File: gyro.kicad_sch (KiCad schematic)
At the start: 0 parts

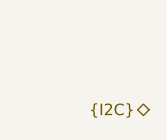
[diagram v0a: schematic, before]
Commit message: Fixed bus names
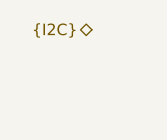
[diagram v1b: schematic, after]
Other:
- title: Pheonix ADXL -> Phoenix Gyro
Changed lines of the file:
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@@
   (paper "A5")
   (title_block
-    (title "Pheonix ADXL")
+    (title "Phoenix Gyro")
   )
-  (hierarchical_label "{I2C}" (shape bidirectional) (at 27.94 29.21 180)
+  (hierarchical_label "{I2C}" (shape bidirectional) (at 21.59 20.32 180)
     (effects (font (size 1.27 1.27)) (justify right))
   )

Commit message: Various updates because I forgot to commit for a while
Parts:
- added C14: 10uF, symbol Device:C
- added C15: 100nF, symbol Device:C
- added U4: I3G4250D, symbol Sensor:I3G4250D
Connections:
- new net +3.3V: C14.1, C15.1, U4.1 (Vdd_IO), U4.15 (RESERVED), U4.16 (VDD), U4.5 (CS)
- new net GND: C14.2, C15.2, U4.10 (RES), U4.11 (RES), U4.12 (RES), U4.13 (GND), U4.4 (SDO/SA0), U4.8 (RES), U4.9 (RES)
- new net Gyro1: U4.7 (INT1)
- new net Gyro2: U4.6 (DRDY/INT2)
- new net SCL: U4.2 (SCL/SPC)
- new net SDA: U4.3 (SDA/SDI/SDO)

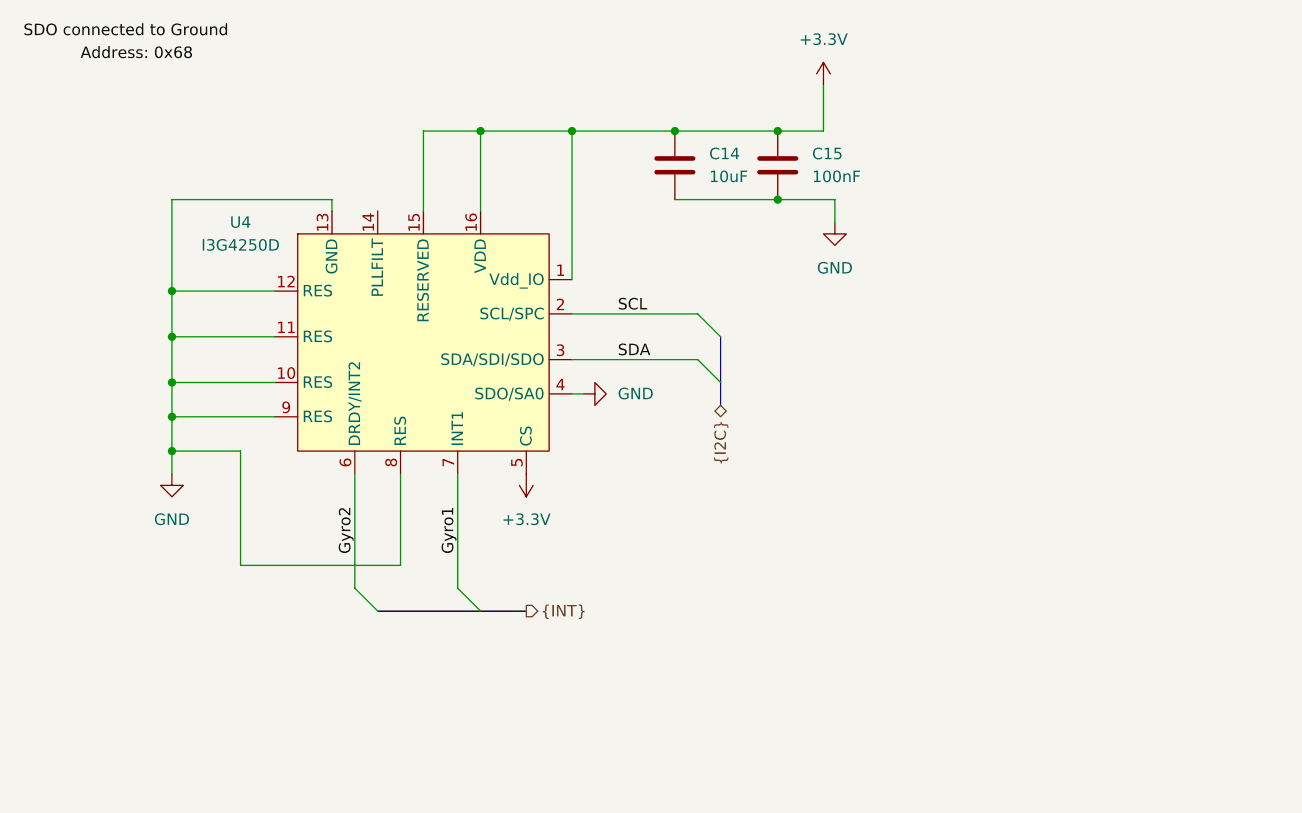
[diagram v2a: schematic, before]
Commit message: Added PLL filter
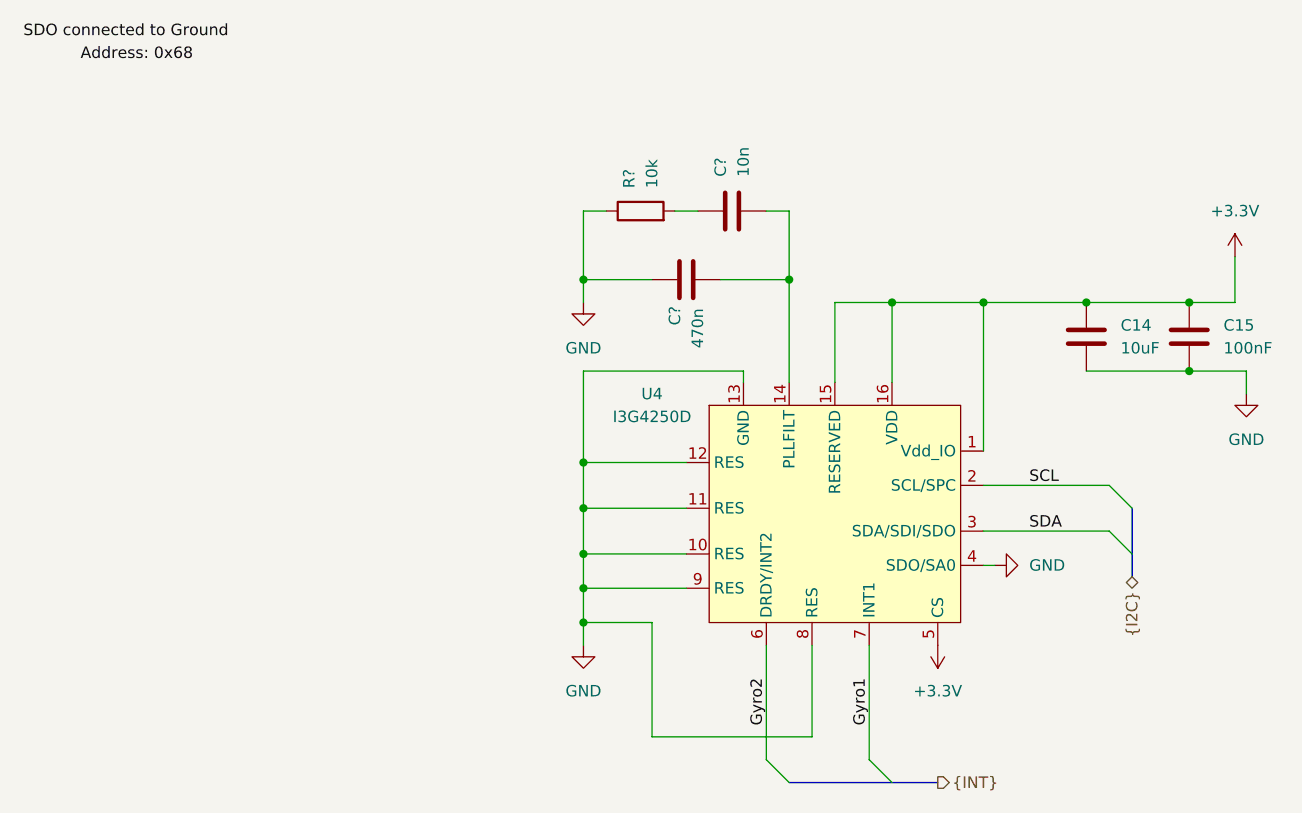
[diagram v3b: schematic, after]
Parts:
- added C?: 470n, Capacitor_SMD:C_0603_1608Metric, symbol Device:C
- added C?: 10n, Capacitor_SMD:C_0603_1608Metric, symbol Device:C
- added R?: 10k, Capacitor_SMD:C_0603_1608Metric, symbol Device:R
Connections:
- net GND: now also C?.1, R?.1
- net at U4.14 (PLLFILT): now also C?.1, C?.2
- new net: C?.2, R?.2
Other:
- moved on the sheet: C14, C15, U4

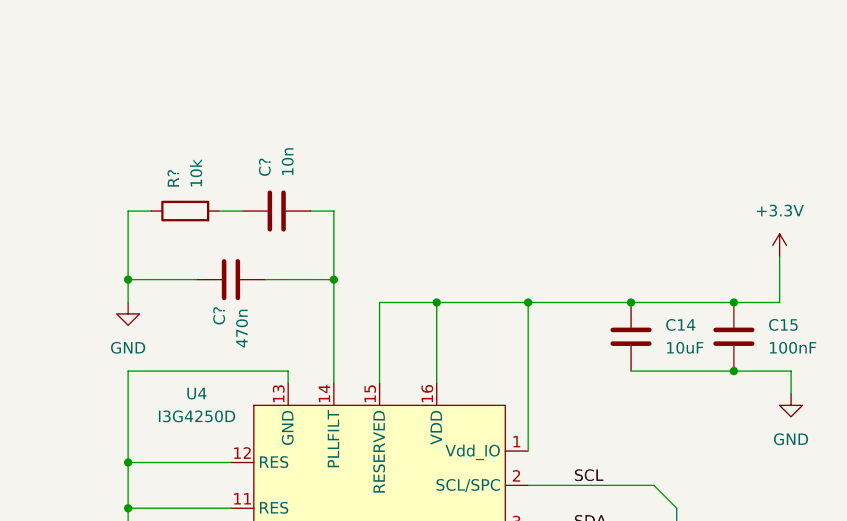
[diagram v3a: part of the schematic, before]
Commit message: Connected the sensors, flash chip, Need to connect the radio and GPS
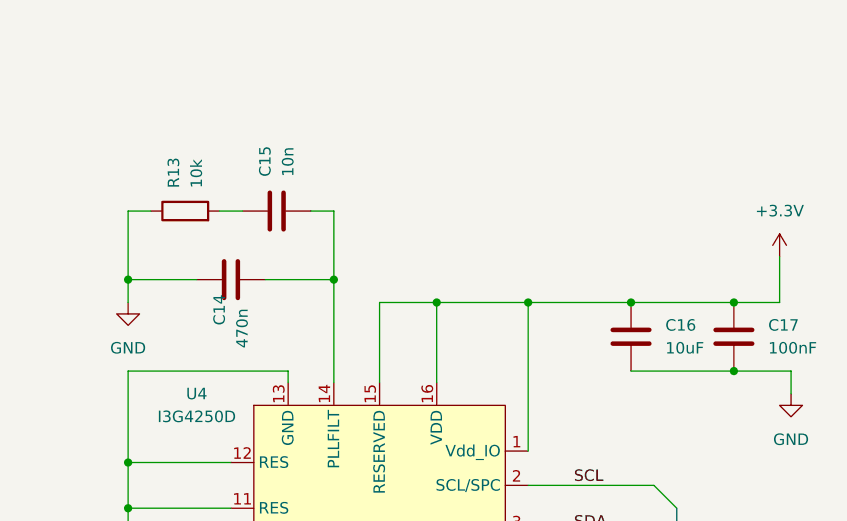
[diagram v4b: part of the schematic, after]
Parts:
- R13: renamed from R?; footprint Capacitor_SMD:C_0603_1608Metric -> Resistor_SMD:R_0603_1608Metric
- U4: footprint (none) -> YAR_Sensors:I3G4250D
- gave numbers to parts that had none: 2
- renumbered C14 to C16, C15 to C17
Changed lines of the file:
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@@
   (symbol (lib_id "power:GND") (at 76.2 83.82 0) (unit 1)
     (in_bom yes) (on_board yes) (fields_autoplaced)
-    (property "Reference" "#PWR027" (id 0) (at 76.2 90.17 0)
+    (property "Reference" "#PWR029" (id 0) (at 76.2 90.17 0)
       (effects (font (size 1.27 1.27)) hide)
     )
@@
   (symbol (lib_id "Device:C") (at 143.51 49.53 0) (unit 1)
     (in_bom yes) (on_board yes)
-    (property "Reference" "C15" (id 0) (at 147.32 48.26 0)
+    (property "Reference" "C17" (id 0) (at 147.32 48.26 0)
       (effects (font (size 1.27 1.27)) (justify left))
     )
@@
   (symbol (lib_id "power:GND") (at 76.2 45.72 0) (unit 1)
     (in_bom yes) (on_board yes) (fields_autoplaced)
-    (property "Reference" "#PWR?" (id 0) (at 76.2 52.07 0)
+    (property "Reference" "#PWR028" (id 0) (at 76.2 52.07 0)
       (effects (font (size 1.27 1.27)) hide)
     )
@@
   (symbol (lib_id "Device:C") (at 132.08 49.53 0) (unit 1)
     (in_bom yes) (on_board yes)
-    (property "Reference" "C14" (id 0) (at 135.89 48.26 0)
+    (property "Reference" "C16" (id 0) (at 135.89 48.26 0)
       (effects (font (size 1.27 1.27)) (justify left))
     )
@@
   (symbol (lib_id "Device:C") (at 87.63 43.18 90) (mirror x) (unit 1)
     (in_bom yes) (on_board yes)
-    (property "Reference" "C?" (id 0) (at 86.36 48.26 0)
+    (property "Reference" "C14" (id 0) (at 86.36 48.26 0)
       (effects (font (size 1.27 1.27)) (justify right))
     )
@@
   (symbol (lib_id "power:GND") (at 149.86 55.88 0) (unit 1)
     (in_bom yes) (on_board yes) (fields_autoplaced)
-    (property "Reference" "#PWR031" (id 0) (at 149.86 62.23 0)
+    (property "Reference" "#PWR033" (id 0) (at 149.86 62.23 0)
       (effects (font (size 1.27 1.27)) hide)
     )
@@
   (symbol (lib_id "Device:C") (at 92.71 35.56 270) (unit 1)
     (in_bom yes) (on_board yes) (fields_autoplaced)
-    (property "Reference" "C?" (id 0) (at 91.4399 31.75 0)
+    (property "Reference" "C15" (id 0) (at 91.4399 31.75 0)
       (effects (font (size 1.27 1.27)) (justify right))
     )
@@
   (symbol (lib_id "Device:R") (at 82.55 35.56 90) (unit 1)
     (in_bom yes) (on_board yes) (fields_autoplaced)
-    (property "Reference" "R?" (id 0) (at 81.2799 33.02 0)
+    (property "Reference" "R13" (id 0) (at 81.2799 33.02 0)
       (effects (font (size 1.27 1.27)) (justify left))
     )
@@
       (effects (font (size 1.27 1.27)) (justify left))
     )
-    (property "Footprint" "Capacitor_SMD:C_0603_1608Metric" (id 2) (at 82.55 37.338 90)
+    (property "Footprint" "Resistor_SMD:R_0603_1608Metric" (id 2) (at 82.55 37.338 90)
       (effects (font (size 1.27 1.27)) hide)
     )
@@
   (symbol (lib_id "power:+3.3V") (at 148.59 40.64 0) (unit 1)
     (in_bom yes) (on_board yes) (fields_autoplaced)
-    (property "Reference" "#PWR030" (id 0) (at 148.59 44.45 0)
+    (property "Reference" "#PWR032" (id 0) (at 148.59 44.45 0)
       (effects (font (size 1.27 1.27)) hide)
     )
@@
   (symbol (lib_id "power:+3.3V") (at 115.57 83.82 180) (unit 1)
     (in_bom yes) (on_board yes) (fields_autoplaced)
-    (property "Reference" "#PWR028" (id 0) (at 115.57 80.01 0)
+    (property "Reference" "#PWR030" (id 0) (at 115.57 80.01 0)
       (effects (font (size 1.27 1.27)) hide)
     )
@@
     (property "Reference" "U4" (id 0) (at 83.82 55.88 0))
     (property "Value" "I3G4250D" (id 1) (at 83.82 58.42 0))
-    (property "Footprint" "" (id 2) (at 97.79 46.99 0)
+    (property "Footprint" "YAR_Sensors:I3G4250D" (id 2) (at 97.79 46.99 0)
       (effects (font (size 1.27 1.27)) hide)
     )
@@
   (symbol (lib_id "power:GND") (at 121.92 74.93 90) (unit 1)
     (in_bom yes) (on_board yes) (fields_autoplaced)
-    (property "Reference" "#PWR029" (id 0) (at 128.27 74.93 0)
+    (property "Reference" "#PWR031" (id 0) (at 128.27 74.93 0)
       (effects (font (size 1.27 1.27)) hide)
     )

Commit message: Rearrange parts of PCB
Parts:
- C16, C17: footprint (none) -> Capacitor_SMD:C_0603_1608Metric
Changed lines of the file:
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@@
       (effects (font (size 1.27 1.27)) (justify left))
     )
-    (property "Footprint" "" (id 2) (at 144.4752 53.34 0)
+    (property "Footprint" "Capacitor_SMD:C_0603_1608Metric" (id 2) (at 144.4752 53.34 0)
       (effects (font (size 1.27 1.27)) hide)
     )
@@
       (effects (font (size 1.27 1.27)) (justify left))
     )
-    (property "Footprint" "" (id 2) (at 133.0452 53.34 0)
+    (property "Footprint" "Capacitor_SMD:C_0603_1608Metric" (id 2) (at 133.0452 53.34 0)
       (effects (font (size 1.27 1.27)) hide)
     )

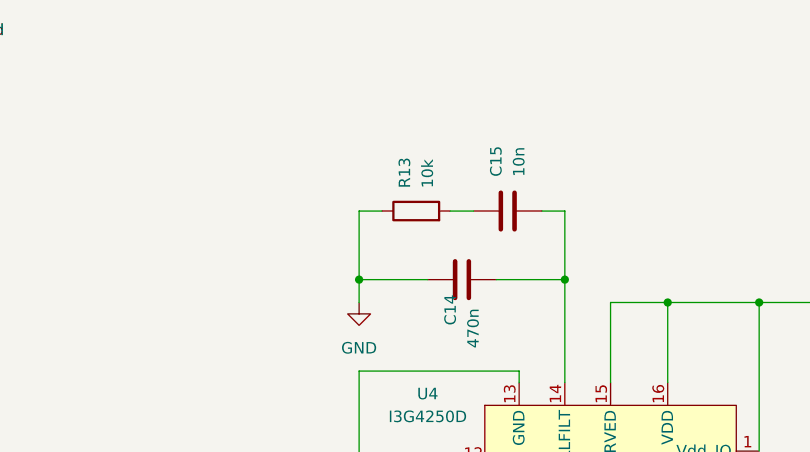
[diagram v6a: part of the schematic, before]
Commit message: Added polyfuse
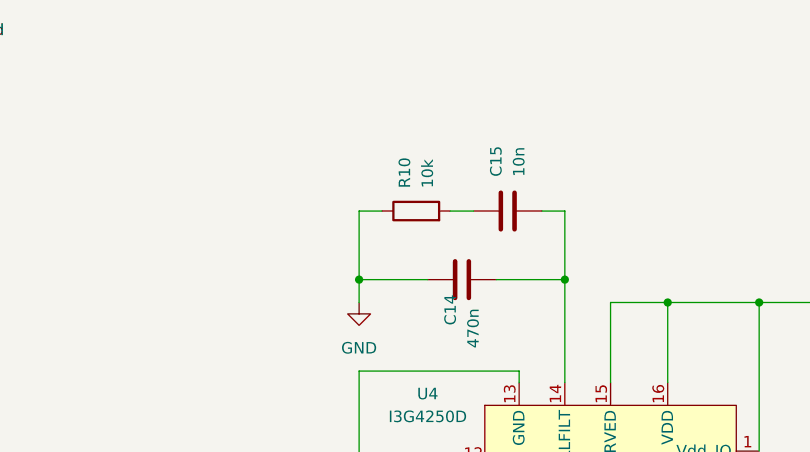
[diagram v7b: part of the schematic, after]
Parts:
- renumbered R13 to R10
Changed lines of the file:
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@@
   (symbol (lib_id "power:GND") (at 76.2 83.82 0) (unit 1)
     (in_bom yes) (on_board yes) (fields_autoplaced)
-    (property "Reference" "#PWR029" (id 0) (at 76.2 90.17 0)
+    (property "Reference" "#PWR027" (id 0) (at 76.2 90.17 0)
       (effects (font (size 1.27 1.27)) hide)
     )
@@
   (symbol (lib_id "power:GND") (at 76.2 45.72 0) (unit 1)
     (in_bom yes) (on_board yes) (fields_autoplaced)
-    (property "Reference" "#PWR028" (id 0) (at 76.2 52.07 0)
+    (property "Reference" "#PWR026" (id 0) (at 76.2 52.07 0)
       (effects (font (size 1.27 1.27)) hide)
     )
@@
   (symbol (lib_id "power:GND") (at 149.86 55.88 0) (unit 1)
     (in_bom yes) (on_board yes) (fields_autoplaced)
-    (property "Reference" "#PWR033" (id 0) (at 149.86 62.23 0)
+    (property "Reference" "#PWR031" (id 0) (at 149.86 62.23 0)
       (effects (font (size 1.27 1.27)) hide)
     )
@@
   (symbol (lib_id "Device:R") (at 82.55 35.56 90) (unit 1)
     (in_bom yes) (on_board yes) (fields_autoplaced)
-    (property "Reference" "R13" (id 0) (at 81.2799 33.02 0)
+    (property "Reference" "R10" (id 0) (at 81.2799 33.02 0)
       (effects (font (size 1.27 1.27)) (justify left))
     )
@@
   (symbol (lib_id "power:+3.3V") (at 148.59 40.64 0) (unit 1)
     (in_bom yes) (on_board yes) (fields_autoplaced)
-    (property "Reference" "#PWR032" (id 0) (at 148.59 44.45 0)
+    (property "Reference" "#PWR030" (id 0) (at 148.59 44.45 0)
       (effects (font (size 1.27 1.27)) hide)
     )
@@
   (symbol (lib_id "power:+3.3V") (at 115.57 83.82 180) (unit 1)
     (in_bom yes) (on_board yes) (fields_autoplaced)
-    (property "Reference" "#PWR030" (id 0) (at 115.57 80.01 0)
+    (property "Reference" "#PWR028" (id 0) (at 115.57 80.01 0)
       (effects (font (size 1.27 1.27)) hide)
     )
@@
   (symbol (lib_id "power:GND") (at 121.92 74.93 90) (unit 1)
     (in_bom yes) (on_board yes) (fields_autoplaced)
-    (property "Reference" "#PWR031" (id 0) (at 128.27 74.93 0)
+    (property "Reference" "#PWR029" (id 0) (at 128.27 74.93 0)
       (effects (font (size 1.27 1.27)) hide)
     )

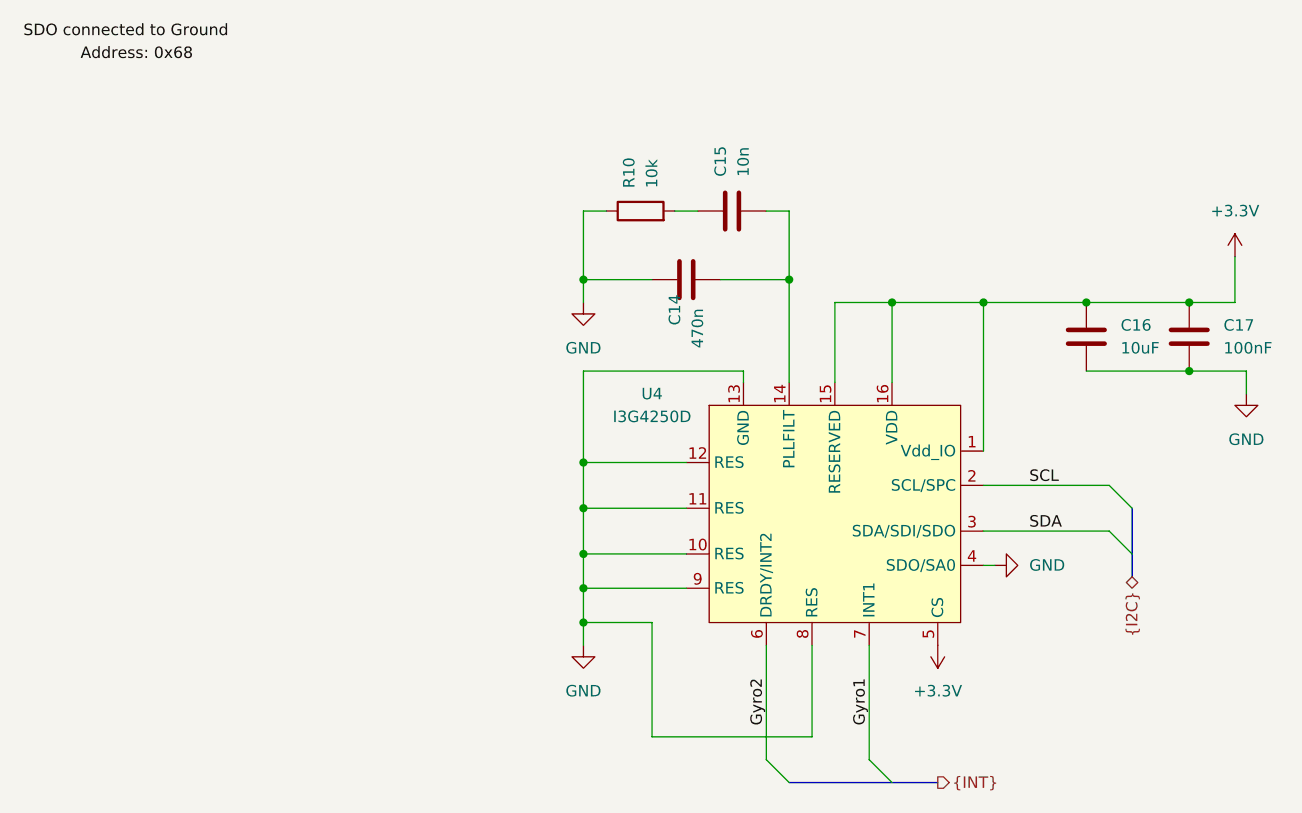
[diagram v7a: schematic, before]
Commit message: Fixed power ports
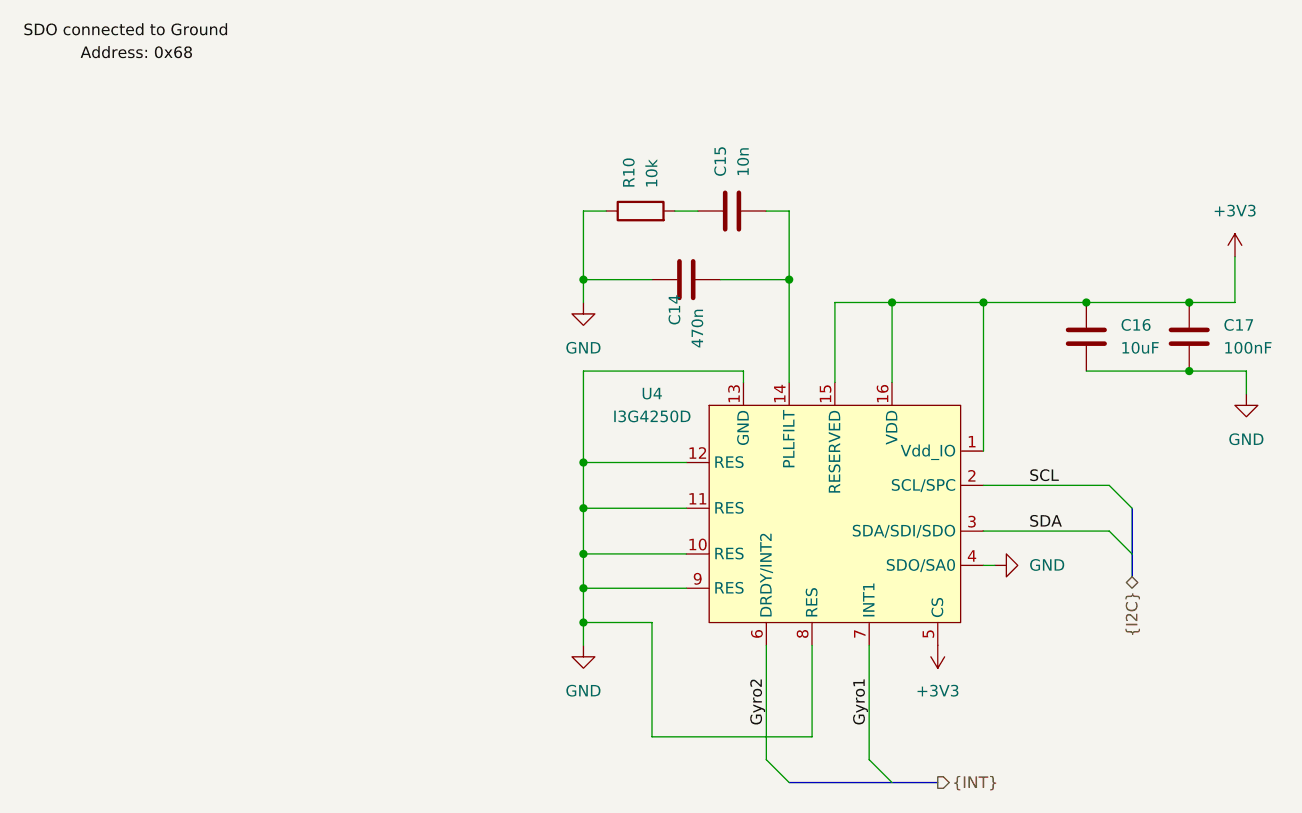
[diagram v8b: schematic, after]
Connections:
- net +3.3V renamed +3V3
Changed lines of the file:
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@@
     (pin "2")
+  )
+  (symbol (lib_id "power:+3V3") (at 115.57 83.82 180) (unit 1)
+    (in_bom yes) (on_board yes) (fields_autoplaced)
+    (property "Reference" "#PWR0101" (id 0) (at 115.57 80.01 0)
+      (effects (font (size 1.27 1.27)) hide)
+    )
+    (property "Value" "+3V3" (id 1) (at 115.57 88.9 0))
+    (property "Footprint" "" (id 2) (at 115.57 83.82 0)
+      (effects (font (size 1.27 1.27)) hide)
+    )
+    (property "Datasheet" "" (id 3) (at 115.57 83.82 0)
+      (effects (font (size 1.27 1.27)) hide)
+    )
+    (pin "1")
+  )
+  (symbol (lib_id "power:+3V3") (at 148.59 40.64 0) (unit 1)
+    (in_bom yes) (on_board yes) (fields_autoplaced)
+    (property "Reference" "#PWR0102" (id 0) (at 148.59 44.45 0)
+      (effects (font (size 1.27 1.27)) hide)
+    )
+    (property "Value" "+3V3" (id 1) (at 148.59 35.56 0))
+    (property "Footprint" "" (id 2) (at 148.59 40.64 0)
+      (effects (font (size 1.27 1.27)) hide)
+    )
+    (property "Datasheet" "" (id 3) (at 148.59 40.64 0)
+      (effects (font (size 1.27 1.27)) hide)
+    )
+    (pin "1")
   )
   (symbol (lib_id "Device:C") (at 87.63 43.18 90) (mirror x) (unit 1)
@@
     (pin "2")
   )
-  (symbol (lib_id "power:+3.3V") (at 148.59 40.64 0) (unit 1)
-    (in_bom yes) (on_board yes) (fields_autoplaced)
-    (property "Reference" "#PWR030" (id 0) (at 148.59 44.45 0)
-      (effects (font (size 1.27 1.27)) hide)
-    )
-    (property "Value" "+3.3V" (id 1) (at 148.59 35.56 0))
-    (property "Footprint" "" (id 2) (at 148.59 40.64 0)
-      (effects (font (size 1.27 1.27)) hide)
-    )
-    (property "Datasheet" "" (id 3) (at 148.59 40.64 0)
-      (effects (font (size 1.27 1.27)) hide)
-    )
-    (pin "1")
-  )
-  (symbol (lib_id "power:+3.3V") (at 115.57 83.82 180) (unit 1)
-    (in_bom yes) (on_board yes) (fields_autoplaced)
-    (property "Reference" "#PWR028" (id 0) (at 115.57 80.01 0)
-      (effects (font (size 1.27 1.27)) hide)
-    )
-    (property "Value" "+3.3V" (id 1) (at 115.57 88.9 0))
-    (property "Footprint" "" (id 2) (at 115.57 83.82 0)
-      (effects (font (size 1.27 1.27)) hide)
-    )
-    (property "Datasheet" "" (id 3) (at 115.57 83.82 0)
-      (effects (font (size 1.27 1.27)) hide)
-    )
-    (pin "1")
-  )
   (symbol (lib_id "Sensor:I3G4250D") (at 97.79 46.99 0) (unit 1)
